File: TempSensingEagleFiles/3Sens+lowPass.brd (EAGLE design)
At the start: 34.5 x 34 mm, 7 parts, among them U3 MLX90614_

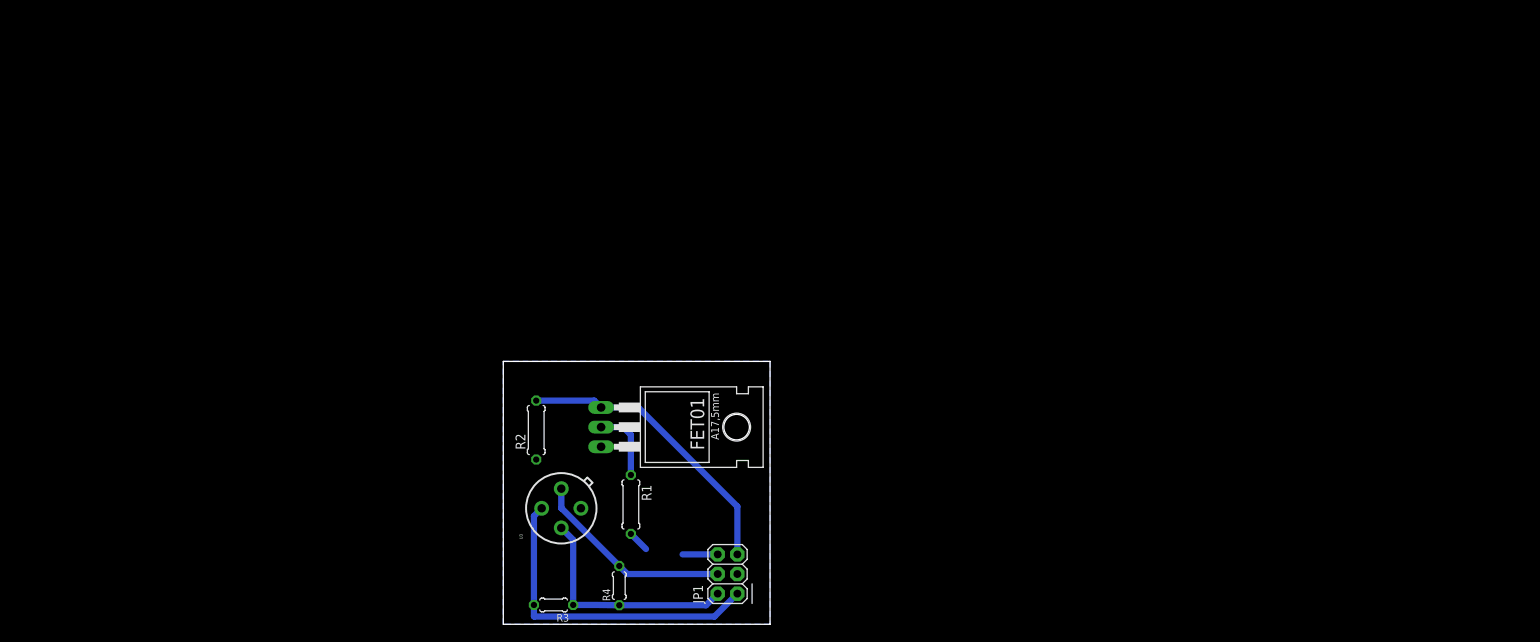
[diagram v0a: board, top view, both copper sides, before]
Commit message: worked on Eagle Files
Added 1 Sensor and Main board
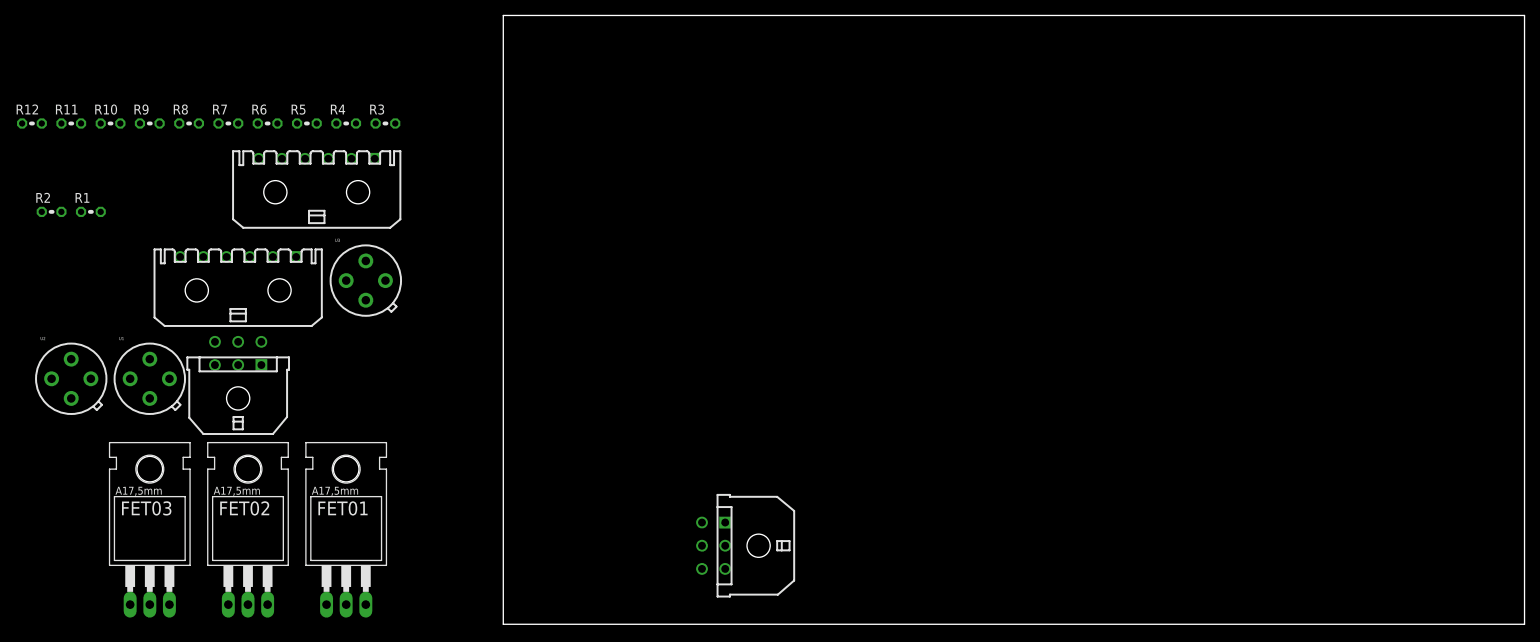
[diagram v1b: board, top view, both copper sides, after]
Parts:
- removed JP1: (no value), SparkFun-Connectors:2X03
- added FET02, FET03: IRF3710, transistor-power:TO220AH
- added R10, R11, R12, R7, R8, R9: 4.1k, resistor:0204V
- added R5, R6: 10k, resistor:0204V
- added U1, U2: MLX90614_, SparkFun-Sensors:TO-39
- added X1, X2: (no value), con-molex-micro-fit-3_0:43045-0600
- added X3, X4: (no value), con-molex-micro-fit-3_0:43650-0600
- R1: device rcl:0207/7 -> resistor:0204V
- R2: value 10k -> 12h; device rcl:0207/7 -> resistor:0204V
- R3: value 4.1k -> 6.8h; device rcl:0204/5 -> resistor:0204V
- R4: value 4.1k -> 10k; device rcl:0204/5 -> resistor:0204V
- moved R1 79.4 mm to (-53.3, 53.3), turned to 0 degrees
- moved R4 69.4 mm to (-20.3, 64.8), turned to 0 degrees
- moved R2 68.7 mm to (-58.4, 53.3), turned to 0 degrees
- moved R3 66.0 mm to (-15.2, 64.8), turned to 0 degrees
- moved FET01 42.7 mm to (-20.3, 8.89), turned to 0 degrees
- moved U3 38.8 mm to (-17.8, 44.5), turned to 0 degrees
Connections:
- removed net N$18 (its old number): FET01.B, JP1.5, R2.2
- new net +3V3: R10.1, R11.1, R12.1, R7.1, R8.1, R9.1, U1.3, U2.3, U3.3, X1.P$1
- new net N$10: R2.2
- new net N$12: R10.2, U2.1
- new net N$13: R9.2, U2.2
- new net N$14: FET03.C, R3.1
- new net N$17: FET02.C, R2.1
- new net N$3: FET02.B, R5.2
- new net N$4: FET02.E, R5.1
- new net N$5: FET01.B, R6.2
- new net N$6: FET01.E, R6.1
- new net N$8: R7.2, U1.2, X1.P$6
- new net N$9: FET03.B, R4.2, X1.P$3
- new net VCC: FET03.E, R4.1
- net GND: now also R3.2, U1.4, U2.4, X1.P$2; no longer FET01.E, JP1.3, R2.1
- net N$1: now also R8.2, U1.1, X1.P$5; no longer JP1.2, R3.1, R4.1, U3.3
- net N$11: no longer JP1.6
- net N$15: now also R11.2; no longer JP1.4, R4.2
- net N$16: now also R12.2; no longer JP1.1, R3.2
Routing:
- net N$16: track 41.9 -> 0.00 mm
- net N$18 (its old number): track 37.9 -> 0.00 mm
- net N$1: track 29.9 -> 0.00 mm
- net N$15: track 26.3 -> 0.00 mm
- net N$18: track 9.45 -> 0.00 mm
- net N$11: track 7.31 -> 0.00 mm
- removed copper zone on layer 16, net GND
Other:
- board size 34.5 x 34 mm -> 132.1 x 78.7 mm
- board text removed: "GND"
- board text removed: "SDA"
- board text removed: "VCC ioio"
- board text removed: "ioio pin"
- board text removed: "scl"
- board text removed: "vib"
